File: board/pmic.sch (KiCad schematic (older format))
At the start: 59 parts, among them J11 DB9, J12 RJ45, P48 CONN_6, P50 CONN_16X2, P51 CONN_4, U17 MAX4377, U18 MAX4378, U19 PIC18F85J94, U20 MAX3227, U21 MAX3490, X2 CRYSTAL

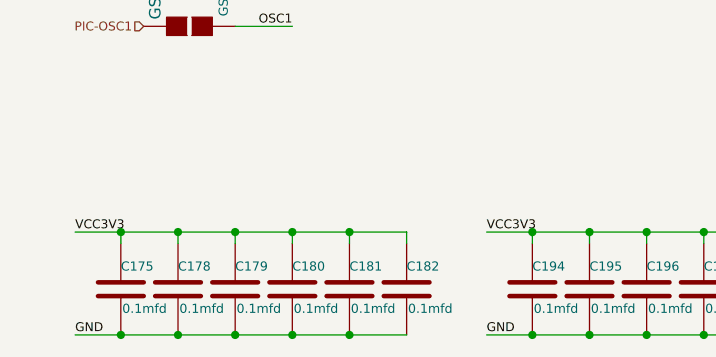
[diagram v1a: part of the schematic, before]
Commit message: Issue #1082 - DRC clearing
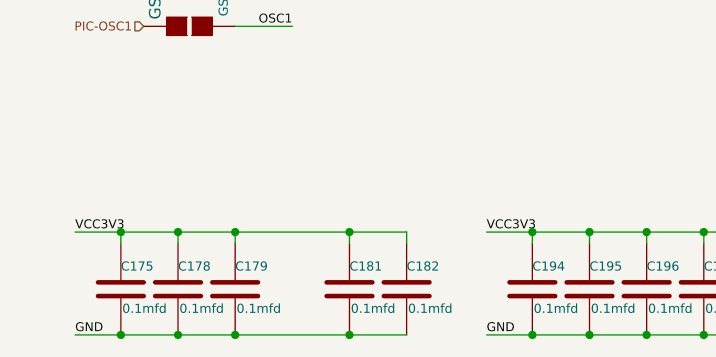
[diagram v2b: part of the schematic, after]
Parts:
- removed C180: 0.1mfd, ~, symbol C
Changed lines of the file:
@@
 LIBS:contrib
 LIBS:valves
+LIBS:xc6slx9-csg324
 LIBS:hdmi2usb
+LIBS:cypress-fx2
 LIBS:hdmi2usb-cache
 EELAYER 27 0
@@
 Sheet 7 8
 Title "HDMI2USB"
-Date "2 may 2014"
+Date "5 may 2014"
 Rev ""
 Comp ""
@@
 Text Label 5200 9100 1    39   ~ 0
 VCC3V3
-$Comp
-L C C180
-U 1 1 53284A8A
-P 1800 10700
-F 0 "C180" H 1800 10800 40  0000 L CNN
-F 1 "0.1mfd" H 1806 10615 40  0000 L CNN
-F 2 "~" H 1838 10550 30  0000 C CNN
-F 3 "~" H 1800 10700 60  0000 C CNN
-	1    1800 10700
-	1    0    0    -1
-$EndComp
 $Comp
 L C C181
@@
 	1500 6600 2100 6600
 Connection ~ 2050 10900
-Connection ~ 1800 10900
 Connection ~ 1550 10900
 Connection ~ 2050 10450
 Wire Wire Line
 	2300 10450 2300 10500
-Connection ~ 1800 10450
 Wire Wire Line
 	2050 10450 2050 10500
 Connection ~ 1550 10450
 Wire Wire Line
-	1800 10450 1800 10500
-Wire Wire Line
 	5350 8850 5350 9100
